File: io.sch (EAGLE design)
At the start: 34 parts, among them J1 SJ-3523-SMT-TR, Q1 MMBT2222A, Q2 2SCR574D3TL1TRANS_2SCR573_TO-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, U1 MCP1703T-5002E, U3 LM386M-1

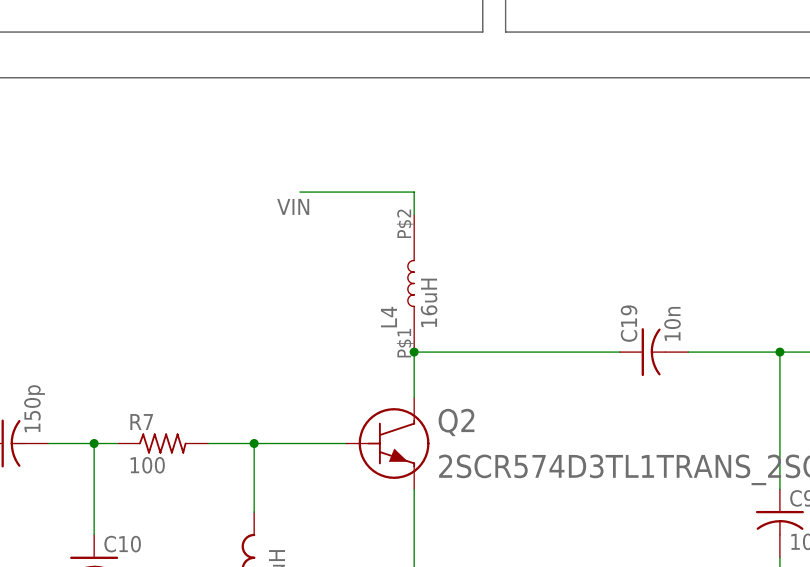
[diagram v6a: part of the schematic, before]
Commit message: Working on 1.1a of I/O after testing
* replaced L4 with a much smaller component
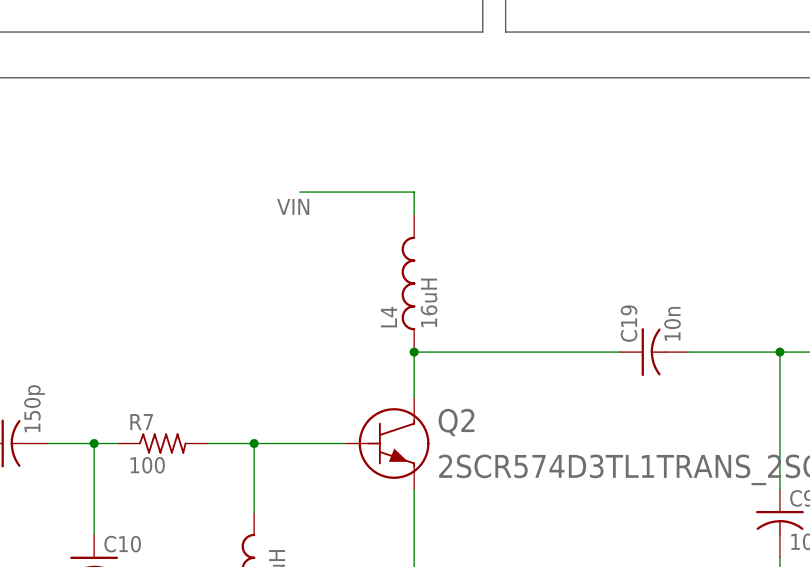
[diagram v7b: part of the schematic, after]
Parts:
- L4: device zort2:B966AS-160M-P3 -> LQW18AN16NG8ZD:LQW18AN16NG8ZD
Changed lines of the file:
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@@
 <?xml version="1.0" encoding="utf-8"?>
 <!DOCTYPE eagle SYSTEM "eagle.dtd">
-<eagle version="9.6.1">
+<eagle version="9.6.2">
 <drawing>
 <settings>
@@
 <part name="JP1" library="adafruit" library_urn="urn:adsk.eagle:library:420" deviceset="PINHD-2X4" device="" package3d_urn="urn:adsk.eagle:package:6240893/1"/>
 <part name="L5" library="Inductor" library_urn="urn:adsk.eagle:library:16378440" deviceset="L" device="CHIP-0805(2012-METRIC)" package3d_urn="urn:adsk.eagle:package:16378480/1" technology="_" value="1.2uH"/>
-<part name="L4" library="zort2" deviceset="B966AS-160M-P3" device="" value="16uH"/>
+<part name="L4" library="LQW18AN16NG8ZD" deviceset="LQW18AN16NG8ZD" device="" value="16uH"/>
 <part name="Q1" library="zort2" deviceset="MMBT2222A-7-F" device="SOT-23_DIO-M" value="MMBT2222A"/>
 <part name="U$1" library="zort2" deviceset="9V_968" device="9V_968_SMD"/>

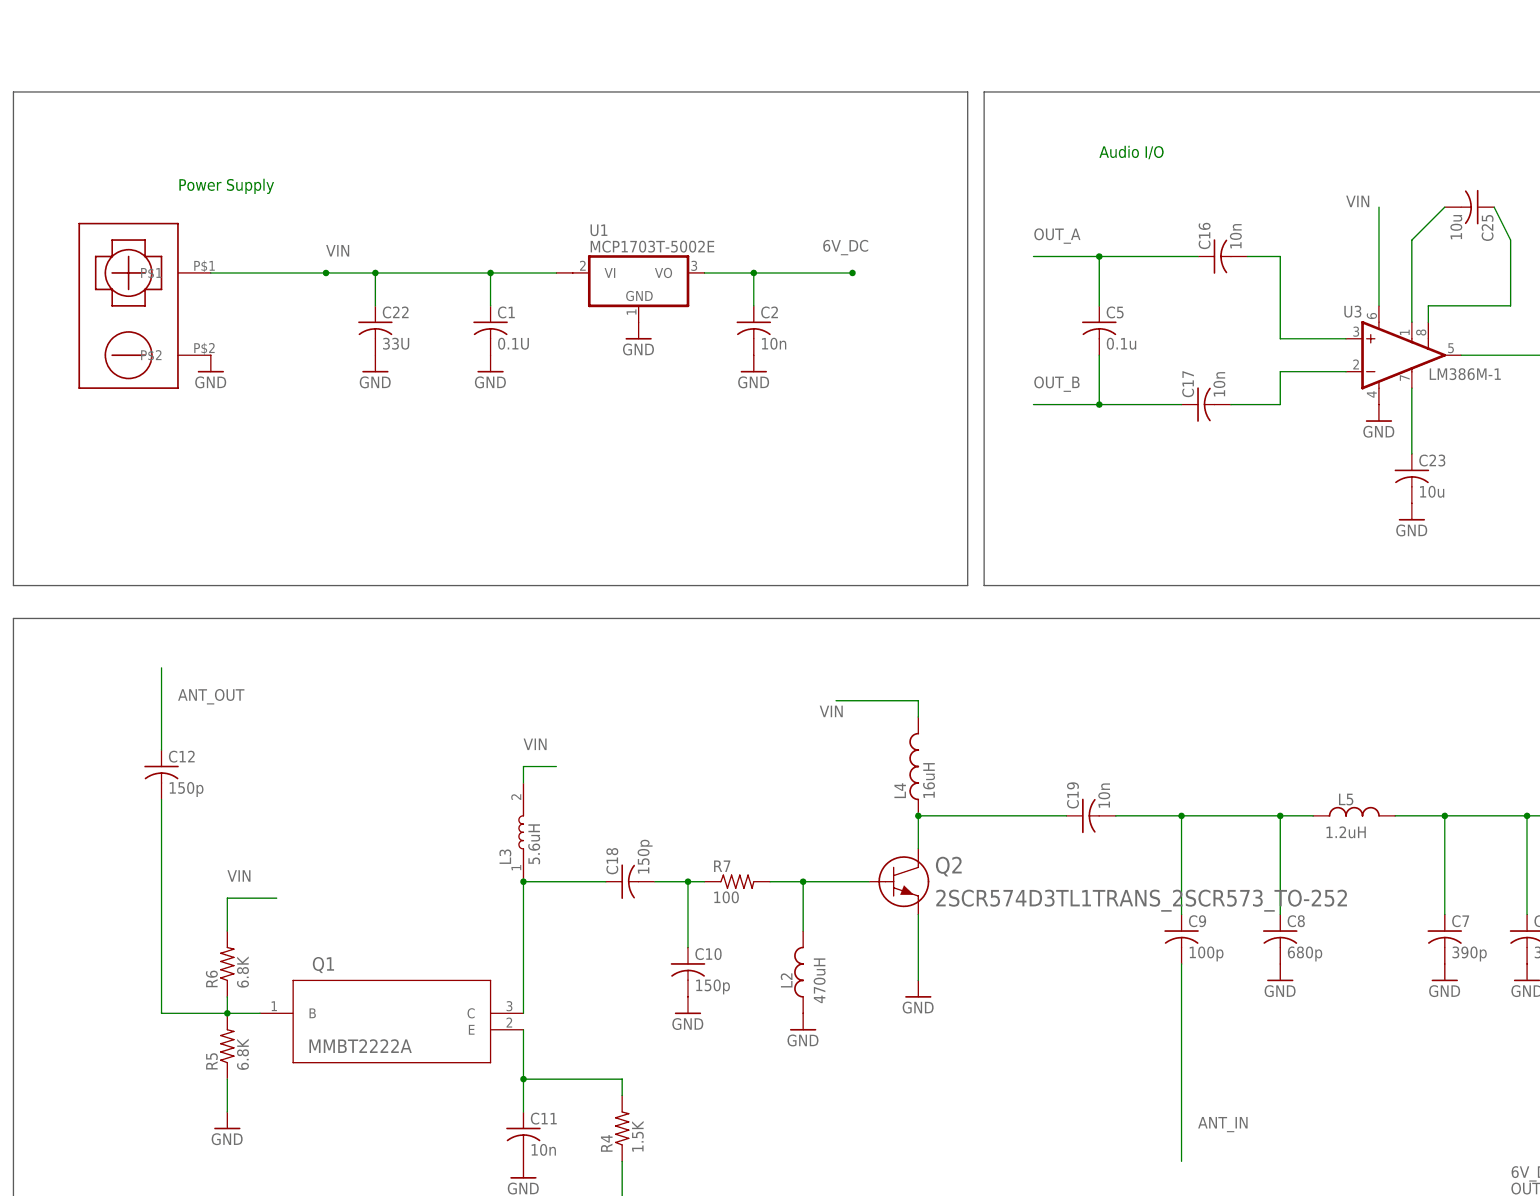
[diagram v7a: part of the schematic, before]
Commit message: Continuing on V1.1a of the I/O board
* re-placed Q1 on the layout
* updated images
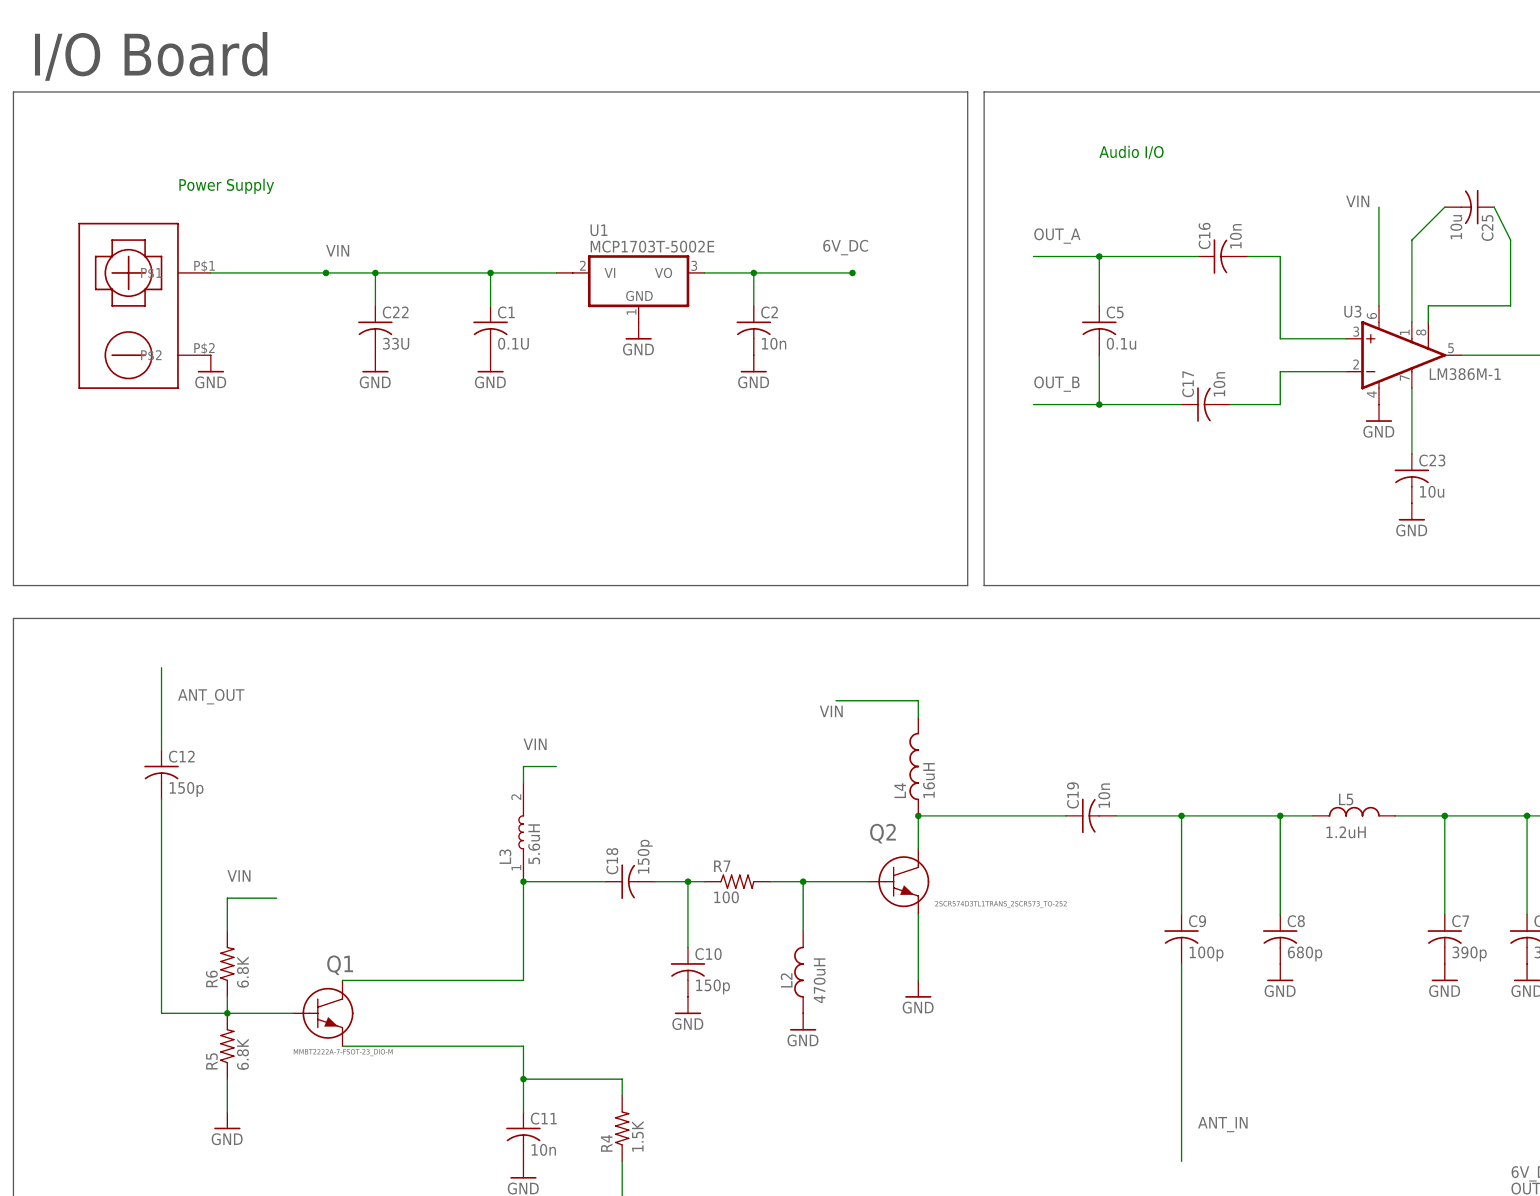
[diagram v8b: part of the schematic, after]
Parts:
- Q1: value MMBT2222A -> MMBT2222A-7-FSOT-23_DIO-M
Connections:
- net N$19: now also Q1.1; no longer Q1.B
- net N$20: now also Q1.3; no longer Q1.E
- net N$21: now also Q1.2; no longer Q1.C
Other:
- note added: "I/O Board"
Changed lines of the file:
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@@
 <part name="L5" library="Inductor" library_urn="urn:adsk.eagle:library:16378440" deviceset="L" device="CHIP-0805(2012-METRIC)" package3d_urn="urn:adsk.eagle:package:16378480/1" technology="_" value="1.2uH"/>
 <part name="L4" library="LQW18AN16NG8ZD" deviceset="LQW18AN16NG8ZD" device="" value="16uH"/>
-<part name="Q1" library="zort2" deviceset="MMBT2222A-7-F" device="SOT-23_DIO-M" value="MMBT2222A"/>
 <part name="U$1" library="zort2" deviceset="9V_968" device="9V_968_SMD"/>
 <part name="Q2" library="zort2" deviceset="2SCR574D3TL1" device="TRANS_2SCR573_TO-252"/>
@@
 <part name="J1" library="SJ-3523-SMT-TR" deviceset="SJ-3523-SMT-TR" device=""/>
 <part name="X1" library="zort2" deviceset="SMACONNECTOR" device="_EDGE" package3d_urn="urn:adsk.eagle:package:6240945/1"/>
+<part name="Q1" library="zort2" deviceset="MMBT2222A-7-F" device="SOT-23_DIO-M"/>
 </parts>
 <sheets>
@@
 <wire x1="50.8" y1="45.72" x2="50.8" y2="121.92" width="0.1524" layer="97"/>
 <wire x1="50.8" y1="121.92" x2="-96.52" y2="121.92" width="0.1524" layer="97"/>
+<text x="-93.98" y="124.46" size="6.4516" layer="97">I/O Board</text>
 </plain>
 <instances>
@@
 <attribute name="VALUE" x="45.72271875" y="12.694559375" size="1.779909375" layer="96" rot="R90"/>
 </instance>
-<instance part="Q1" gate="A" x="-60.96" y="-20.32" smashed="yes">
-<attribute name="NAME" x="-50.4444" y="-13.7414" size="2.0828" layer="95" ratio="6" rot="SR0"/>
-<attribute name="VALUE" x="-51.0794" y="-26.4414" size="2.0828" layer="96" ratio="6" rot="SR0"/>
-</instance>
 <instance part="U$1" gate="G$1" x="-78.74" y="88.9" smashed="yes"/>
 <instance part="Q2" gate="A" x="40.64" y="0" smashed="yes">
-<attribute name="NAME" x="45.72" y="1.27" size="2.54" layer="95" ratio="10" rot="SR0"/>
-<attribute name="VALUE" x="45.72" y="-3.81" size="2.54" layer="96" ratio="10" rot="SR0"/>
+<attribute name="NAME" x="35.56" y="6.35" size="2.54" layer="95" ratio="10" rot="SR0"/>
+<attribute name="VALUE" x="45.72" y="-3.81" size="0.8128" layer="96" ratio="10" rot="SR0"/>
 </instance>
 <instance part="L2" gate="G$1" x="25.4" y="-15.24" smashed="yes" rot="R90">
@@
 <attribute name="NAME" x="170.18" y="12.7" size="1.27" layer="95"/>
 <attribute name="VALUE" x="170.18" y="10.16" size="1.27" layer="95"/>
+</instance>
+<instance part="Q1" gate="G$1" x="-48.26" y="-20.32" smashed="yes">
+<attribute name="NAME" x="-48.26" y="-13.97" size="2.54" layer="95" ratio="10" rot="SR0"/>
+<attribute name="VALUE" x="-53.34" y="-26.67" size="0.8128" layer="96" ratio="10" rot="SR0"/>
 </instance>
 </instances>
@@
 <wire x1="-73.66" y1="-20.32" x2="-63.5" y2="-20.32" width="0.1524" layer="91"/>
 <pinref part="R5" gate="G$1" pin="2"/>
-<wire x1="-63.5" y1="-20.32" x2="-58.42" y2="-20.32" width="0.1524" layer="91"/>
+<wire x1="-63.5" y1="-20.32" x2="-53.34" y2="-20.32" width="0.1524" layer="91"/>
 <junction x="-63.5" y="-20.32"/>
 <pinref part="R6" gate="G$1" pin="1"/>
 <wire x1="-63.5" y1="-20.32" x2="-63.5" y2="-17.78" width="0.1524" layer="91"/>
-<pinref part="Q1" gate="A" pin="B"/>
+<pinref part="Q1" gate="G$1" pin="1"/>
 </segment>
 </net>
@@
 <segment>
 <pinref part="C11" gate="G$1" pin="1"/>
-<wire x1="-17.78" y1="-22.86" x2="-17.78" y2="-30.48" width="0.1524" layer="91"/>
 <junction x="-17.78" y="-30.48"/>
 <wire x1="-17.78" y1="-30.48" x2="-17.78" y2="-35.56" width="0.1524" layer="91"/>
@@
 <pinref part="R4" gate="G$1" pin="2"/>
 <wire x1="-2.54" y1="-30.48" x2="-2.54" y2="-33.02" width="0.1524" layer="91"/>
-<pinref part="Q1" gate="A" pin="E"/>
+<pinref part="Q1" gate="G$1" pin="3"/>
+<wire x1="-45.72" y1="-25.4" x2="-17.78" y2="-25.4" width="0.1524" layer="91"/>
+<wire x1="-17.78" y1="-25.4" x2="-17.78" y2="-30.48" width="0.1524" layer="91"/>
 </segment>
 </net>
@@
 <segment>
 <pinref part="L3" gate="G$1" pin="1"/>
-<wire x1="-17.78" y1="-20.32" x2="-17.78" y2="0" width="0.1524" layer="91"/>
+<wire x1="-17.78" y1="-15.24" x2="-17.78" y2="0" width="0.1524" layer="91"/>
 <pinref part="C18" gate="G$1" pin="1"/>
 <wire x1="-17.78" y1="0" x2="-5.08" y2="0" width="0.1524" layer="91"/>
 <junction x="-17.78" y="0"/>
-<pinref part="Q1" gate="A" pin="C"/>
-</segment>
-</net>
+<pinref part="Q1" gate="G$1" pin="2"/>
+<wire x1="-45.72" y1="-15.24" x2="-17.78" y2="-15.24" width="0.1524" layer="91"/>
+</segment>
+</net>
